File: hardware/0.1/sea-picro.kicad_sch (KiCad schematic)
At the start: 44 parts, among them J1 USB_C_Receptacle_USB2.0, J2 0.1" x 12, J3 0.1" x 12, SW1 BOOT, SW2 RESET, U1 AP2112K-3.3, U3 W25Q128JVSIQ, U4 RP2040, Y1 12MHz

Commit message: add ws2812 3d model
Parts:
- D1: LCSC C122853 -> (none); MPN  B5817WL -> (none); Manufacturer Shikues -> (none)
- J2, J3, LOGO1: now left out of the parts list
- R1, R2, R3: LCSC C14677 -> (none); MPN  RC0603JR-075K1L -> (none); Manufacturer YAGEO -> (none)
- TP1, TP2, TP3, TP4: DNP (none) -> DNP; now left out of the parts list
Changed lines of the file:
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@@
       (effects (font (size 1.27 1.27)) hide)
     )
-    (property "LCSC" "C14677" (id 4) (at 60.325 35.56 0)
-      (effects (font (size 1.27 1.27)) hide)
-    )
-    (property "MPN " "RC0603JR-075K1L" (id 5) (at 60.325 35.56 0)
-      (effects (font (size 1.27 1.27)) hide)
-    )
-    (property "Manufacturer" "YAGEO" (id 6) (at 60.325 35.56 0)
+    (property "LCSC" "" (id 4) (at 60.325 35.56 0)
+      (effects (font (size 1.27 1.27)) hide)
+    )
+    (property "MPN " "" (id 5) (at 60.325 35.56 0)
+      (effects (font (size 1.27 1.27)) hide)
+    )
+    (property "Manufacturer" "" (id 6) (at 60.325 35.56 0)
       (effects (font (size 1.27 1.27)) hide)
     )
@@
       (effects (font (size 1.27 1.27)) hide)
     )
-    (property "LCSC" "C14677" (id 4) (at 60.325 38.1 0)
-      (effects (font (size 1.27 1.27)) hide)
-    )
-    (property "MPN " "RC0603JR-075K1L" (id 5) (at 60.325 38.1 0)
-      (effects (font (size 1.27 1.27)) hide)
-    )
-    (property "Manufacturer" "YAGEO" (id 6) (at 60.325 38.1 0)
+    (property "LCSC" "" (id 4) (at 60.325 38.1 0)
+      (effects (font (size 1.27 1.27)) hide)
+    )
+    (property "MPN " "" (id 5) (at 60.325 38.1 0)
+      (effects (font (size 1.27 1.27)) hide)
+    )
+    (property "Manufacturer" "" (id 6) (at 60.325 38.1 0)
       (effects (font (size 1.27 1.27)) hide)
     )
@@
       (effects (font (size 1.27 1.27)) hide)
     )
-    (property "LCSC" "C122853" (id 4) (at 76.2 30.48 0)
-      (effects (font (size 1.27 1.27)) hide)
-    )
-    (property "MPN " "B5817WL" (id 5) (at 76.2 30.48 0)
-      (effects (font (size 1.27 1.27)) hide)
-    )
-    (property "Manufacturer" "Shikues" (id 6) (at 76.2 30.48 0)
+    (property "LCSC" "" (id 4) (at 76.2 30.48 0)
+      (effects (font (size 1.27 1.27)) hide)
+    )
+    (property "MPN " "" (id 5) (at 76.2 30.48 0)
+      (effects (font (size 1.27 1.27)) hide)
+    )
+    (property "Manufacturer" "" (id 6) (at 76.2 30.48 0)
       (effects (font (size 1.27 1.27)) hide)
     )
@@
   )
   (symbol (lib_id "Connector:Conn_01x12_Male") (at 241.935 78.74 180) (unit 1)
-    (in_bom yes) (on_board yes)
+    (in_bom no) (on_board yes)
     (property "Reference" "J2" (id 0) (at 236.855 57.15 0)
       (effects (font (size 1.27 1.27)) (justify right))
@@
   )
   (symbol (lib_id "Connector:Conn_01x12_Male") (at 249.555 76.2 0) (unit 1)
-    (in_bom yes) (on_board yes)
+    (in_bom no) (on_board yes)
     (property "Reference" "J3" (id 0) (at 249.555 57.15 0))
     (property "Value" "0.1\" x 12" (id 1) (at 253.365 59.69 0))
@@
       (effects (font (size 1.27 1.27)) hide)
     )
-    (property "LCSC" "C14677" (id 4) (at 231.14 119.38 0)
-      (effects (font (size 1.27 1.27)) hide)
-    )
-    (property "MPN " "RC0603JR-075K1L" (id 5) (at 231.14 119.38 0)
-      (effects (font (size 1.27 1.27)) hide)
-    )
-    (property "Manufacturer" "YAGEO" (id 6) (at 231.14 119.38 0)
+    (property "LCSC" "" (id 4) (at 231.14 119.38 0)
+      (effects (font (size 1.27 1.27)) hide)
+    )
+    (property "MPN " "" (id 5) (at 231.14 119.38 0)
+      (effects (font (size 1.27 1.27)) hide)
+    )
+    (property "Manufacturer" "" (id 6) (at 231.14 119.38 0)
       (effects (font (size 1.27 1.27)) hide)
     )
@@
   )
   (symbol (lib_id "Graphic:Logo_Open_Hardware_Small") (at 161.29 189.23 0) (unit 1)
-    (in_bom yes) (on_board yes)
+    (in_bom no) (on_board yes)
     (property "Reference" "LOGO1" (id 0) (at 161.29 182.245 0)
       (effects (font (size 1.27 1.27)) hide)
@@
   )
   (symbol (lib_id "Connector:TestPoint") (at 65.405 43.815 0) (unit 1)
-    (in_bom yes) (on_board yes)
+    (in_bom no) (on_board yes)
     (property "Reference" "TP1" (id 0) (at 66.8782 40.8178 0)
       (effects (font (size 1.27 1.27)) (justify left))
@@
       (effects (font (size 1.27 1.27)) hide)
     )
+    (property "DNP" "DNP" (id 4) (at 65.405 43.815 0)
+      (effects (font (size 1.27 1.27)) hide)
+    )
     (pin "1")
   )
   (symbol (lib_id "Connector:TestPoint") (at 65.405 50.165 180) (unit 1)
-    (in_bom yes) (on_board yes)
+    (in_bom no) (on_board yes)
     (property "Reference" "TP2" (id 0) (at 66.8782 50.8254 0)
       (effects (font (size 1.27 1.27)) (justify right))
@@
     )
     (property "Datasheet" "~" (id 3) (at 60.325 50.165 0)
+      (effects (font (size 1.27 1.27)) hide)
+    )
+    (property "DNP" "DNP" (id 4) (at 65.405 50.165 0)
       (effects (font (size 1.27 1.27)) hide)
     )
@@
   )
   (symbol (lib_id "Connector:TestPoint") (at 135.89 119.38 90) (unit 1)
-    (in_bom yes) (on_board yes)
+    (in_bom no) (on_board yes)
     (property "Reference" "TP3" (id 0) (at 130.175 119.38 90))
     (property "Value" "SWDCLK" (id 1) (at 132.08 117.475 90))
@@
     )
     (property "Datasheet" "~" (id 3) (at 135.89 114.3 0)
+      (effects (font (size 1.27 1.27)) hide)
+    )
+    (property "DNP" "DNP" (id 4) (at 135.89 119.38 0)
       (effects (font (size 1.27 1.27)) hide)
     )
@@
   )
   (symbol (lib_id "Connector:TestPoint") (at 135.89 121.92 90) (unit 1)
-    (in_bom yes) (on_board yes)
+    (in_bom no) (on_board yes)
     (property "Reference" "TP4" (id 0) (at 130.175 121.92 90))
     (property "Value" "SWDIO" (id 1) (at 131.445 123.825 90))
@@
       (effects (font (size 1.27 1.27)) hide)
     )
+    (property "DNP" "DNP" (id 4) (at 135.89 121.92 0)
+      (effects (font (size 1.27 1.27)) hide)
+    )

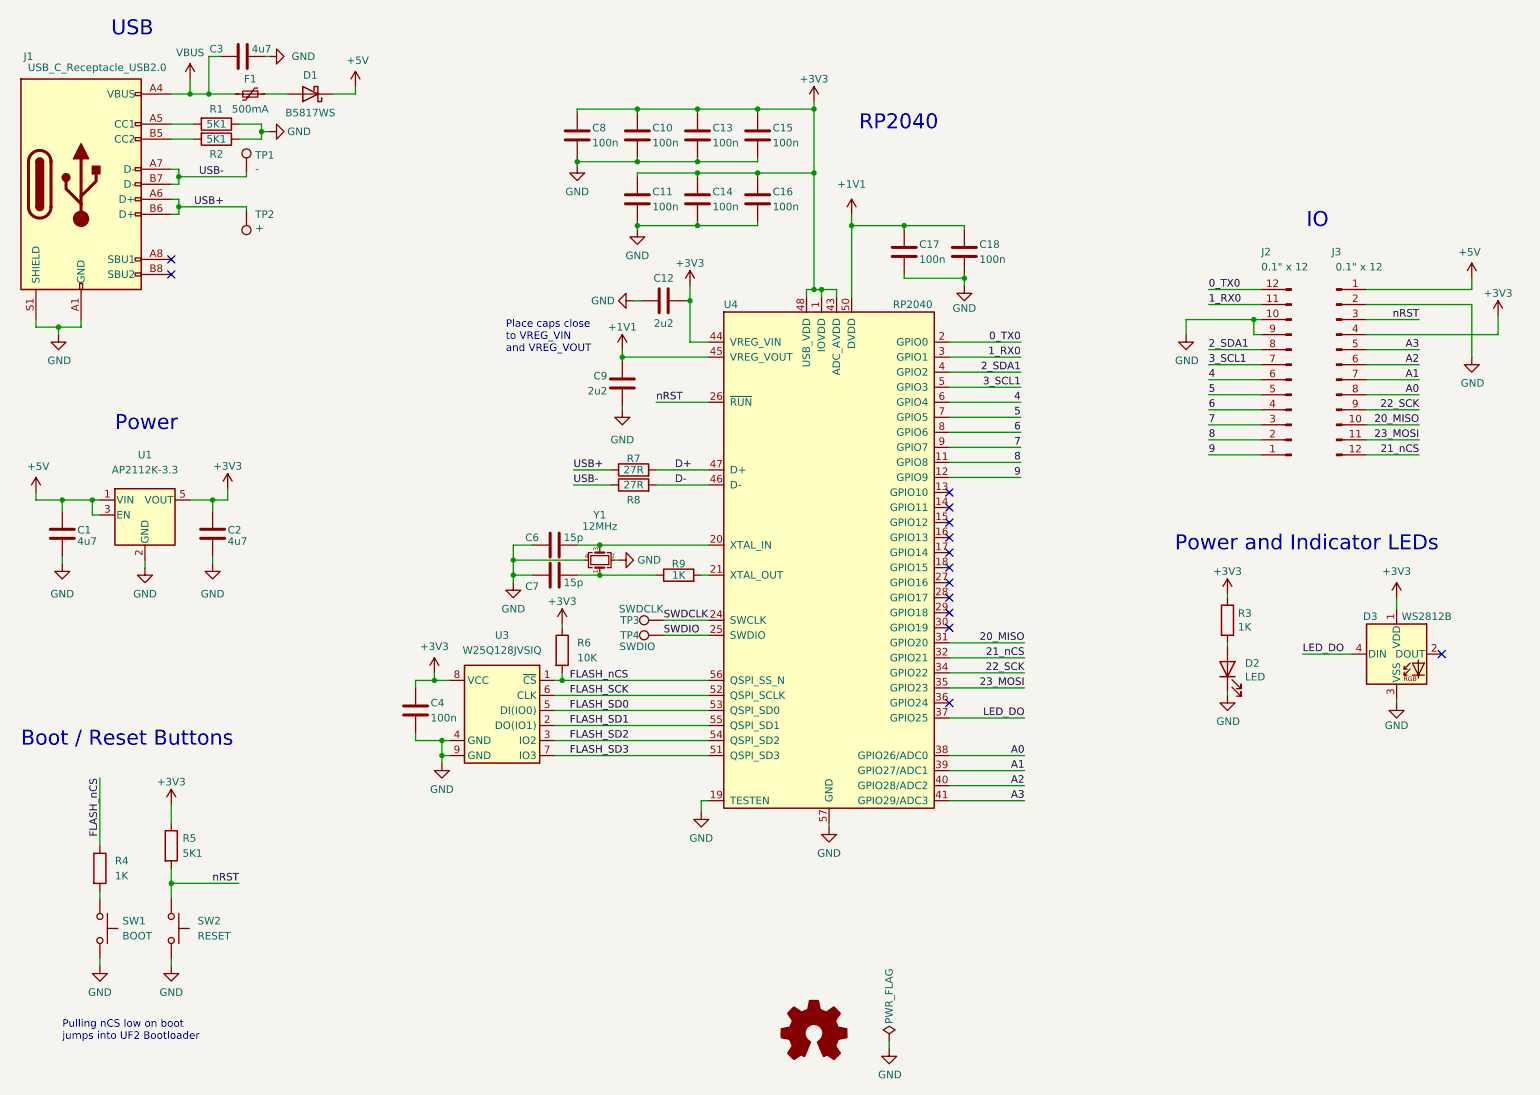
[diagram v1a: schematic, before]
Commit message: clean up traces and add BOM
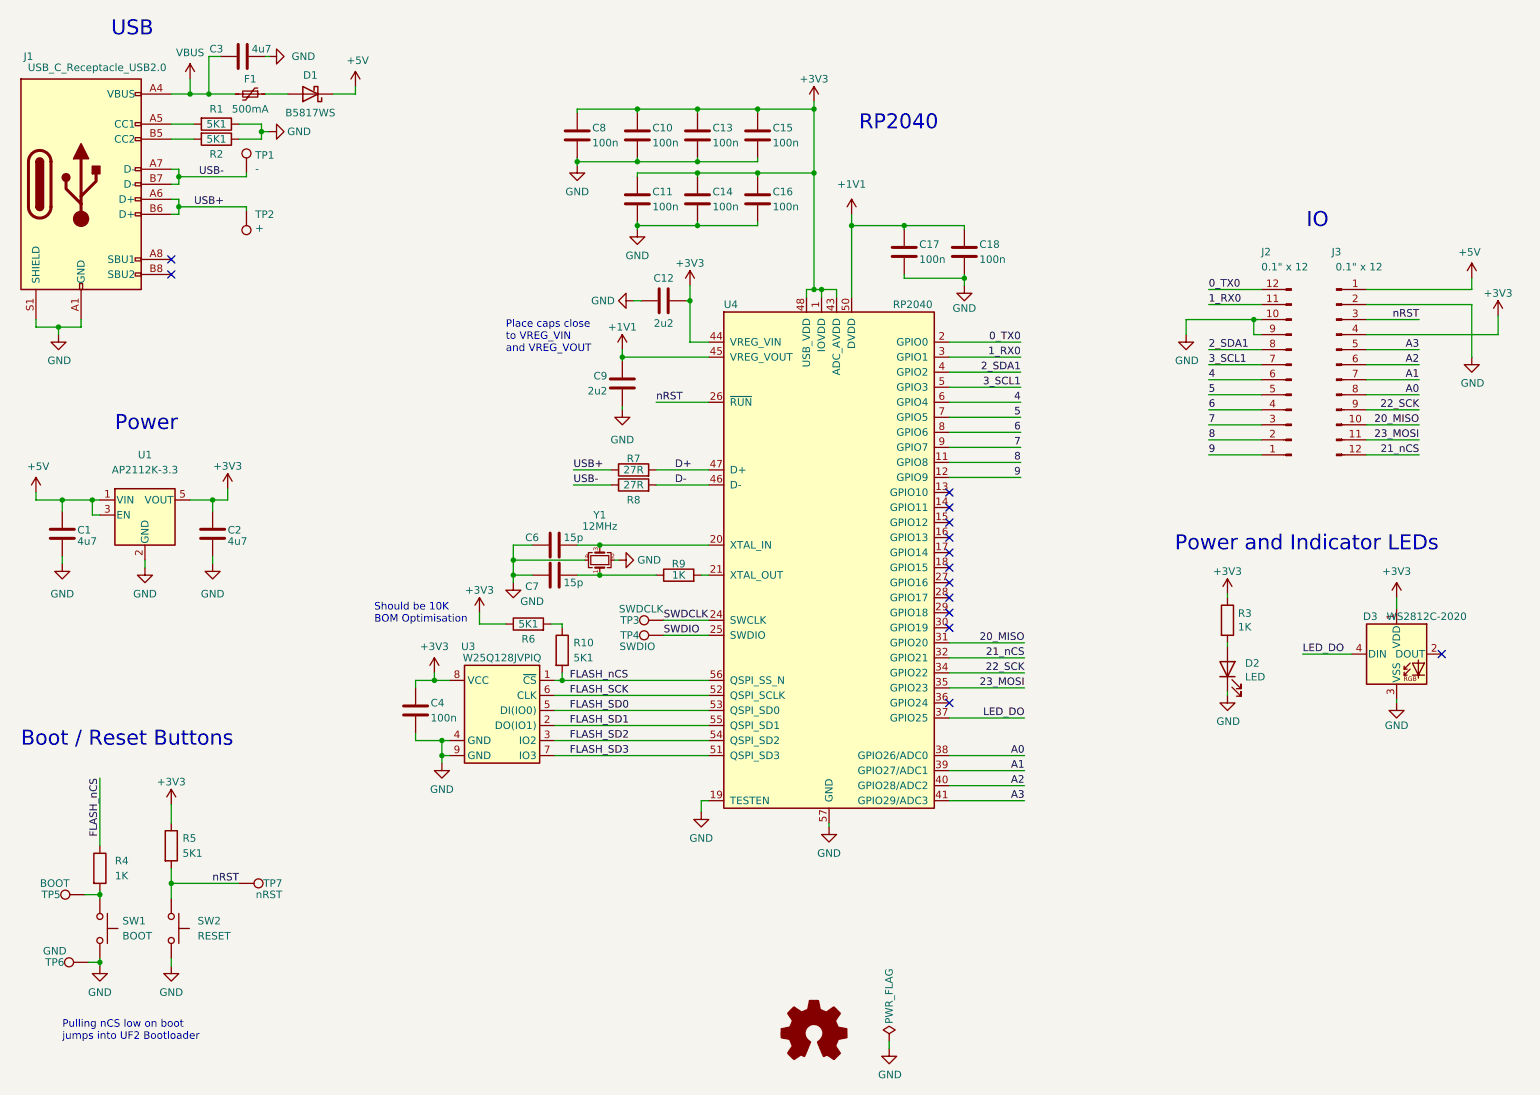
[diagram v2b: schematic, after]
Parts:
- added R10: 5K1, Resistor_SMD:R_0402_1005Metric, symbol Device:R
- added TP5: BOOT, TestPoint:TestPoint_Pad_D1.0mm, symbol Connector:TestPoint
- added TP6: GND, TestPoint:TestPoint_Pad_D1.0mm, symbol Connector:TestPoint
- added TP7: nRST, TestPoint:TestPoint_Pad_D1.0mm, symbol Connector:TestPoint
- C1, C2, C3: LCSC (none) -> C23733; MPN  (none) -> CL05A475MP5NRNC; Manufacturer (none) -> Samsung Electro-Mechanics
- C10, C11, C13, C14, C15, C16, C17, C18, C4, C8: LCSC (none) -> C1525; MPN  (none) -> CL05B104KO5NNNC; Manufacturer (none) -> Samsung Electro-Mechanics
- C12, C9: LCSC (none) -> C12530; MPN  (none) -> CL05A225MQ5NSNC; Manufacturer (none) -> Samsung Electro-Mechanics
- C6, C7: LCSC (none) -> C14445; MPN  (none) -> CL05A105KP5NNNC; Manufacturer (none) -> Samsung Electro-Mechanics
- D1: LCSC (none) -> C699102; MPN  (none) -> B5817WS; Manufacturer (none) -> Yangzhou Yangjie Elec Tech
- D3: value WS2812B -> WS2812C-2020; LCSC (none) -> C965556; MPN  (none) -> WS2812C-2020; Manufacturer (none) -> Worldsemi
- R1, R2, R5: LCSC (none) -> C25905; MPN  (none) -> 0402WGF5101TCE; Manufacturer (none) -> UNI-ROYAL(Uniroyal Elec)
- R3, R4, R9: LCSC (none) -> C11702; MPN  (none) -> 0402WGF1001TCE; Manufacturer (none) -> UNI-ROYAL(Uniroyal Elec)
- R6: value 10K -> 5K1; LCSC (none) -> C25905; MPN  (none) -> 0402WGF5101TCE; Manufacturer (none) -> UNI-ROYAL(Uniroyal Elec)
- R7, R8: LCSC (none) -> C25100; MPN  (none) -> 0402WGF270JTCE; Manufacturer (none) -> UNI-ROYAL(Uniroyal Elec)
- SW1, SW2: LCSC (none) -> C231329; MPN  (none) -> B3U-1000P; Manufacturer (none) -> Omron Electronics
- U1: LCSC (none) -> C51118; MPN  (none) -> AP2112K-3.3TRG1; Manufacturer (none) -> Diodes Incorporated
- U3: value W25Q128JVSIQ -> W25Q128JVPIQ; LCSC (none) -> C190862; MPN  (none) -> W25Q128JVPIQ; Manufacturer (none) -> Winbond Elec
- U4: LCSC (none) -> C2040; MPN  (none) -> RP2040; Manufacturer (none) -> Raspberry Pi
- Y1: LCSC (none) -> C90603; MPN  (none) -> Q24FA20H0068700; Manufacturer (none) -> Seiko Epson
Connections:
- net FLASH_nCS: now also R10.2; no longer R6.2
- net GND: now also TP6.1
- net nRST: now also TP7.1
- net at R4.2, SW1.1: now also TP5.1
- new net: R10.1, R6.2
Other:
- note added: "Should be 10K BOM Optimisation"

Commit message: update dates and revision number
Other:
- company: Josh Johnson and Custom KBD -> Josh Johnson
- title: Sea Micro -> Sea Picro
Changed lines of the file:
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@@
   (paper "A4")
   (title_block
-    (title "Sea Micro")
-    (date "2020-12-11")
-    (rev "0.3")
-    (company "Josh Johnson and Custom KBD")
+    (title "Sea Picro")
+    (date "2022-01-07")
+    (rev "0.1")
+    (company "Josh Johnson")
   )
   (junction (at 140.335 65.405) (diameter 0) (color 0 0 0 0)
